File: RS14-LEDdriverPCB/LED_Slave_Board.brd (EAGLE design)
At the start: 63.2 x 38.1 mm, 26 parts, among them U1 PIC32MX250F128B-I/SP

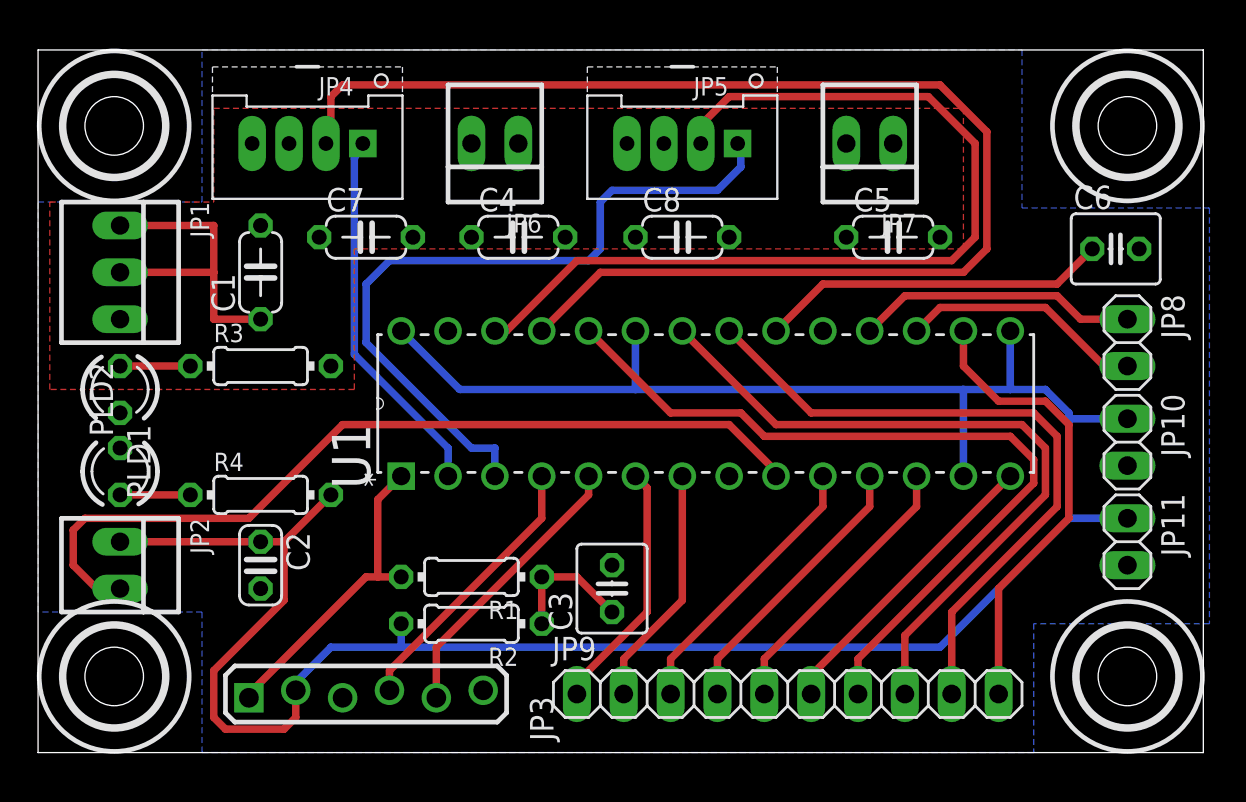
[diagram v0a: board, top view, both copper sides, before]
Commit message: Revised Board and Schematic
Changed capacitor footprints and screw hole placement
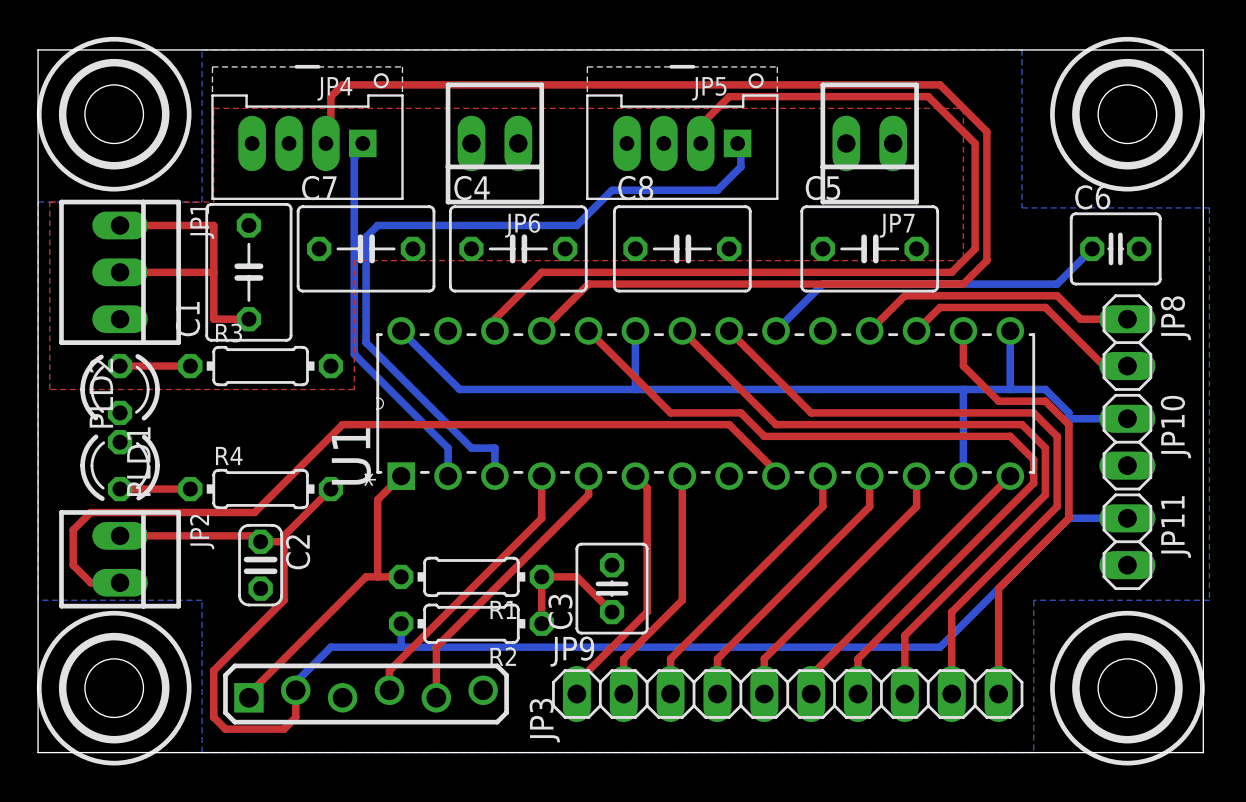
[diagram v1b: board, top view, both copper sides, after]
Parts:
- C1, C4, C5, C7, C8: device rcl:C050-024X044 -> rcl:C050-045X075
- moved C5 1.42 mm to (45.1, 27.3)
- moved C4 0.64 mm to (26.0, 27.3)
- moved C7 0.64 mm to (17.8, 27.3)
- moved C8 0.64 mm to (34.9, 27.3)
- moved C1 0.63 mm to (11.4, 26.0)
- moved JP2 0.32 mm to (4.45, 10.5)
- moved PLD2 0.32 mm to (4.45, 15.6)
- moved R4 0.32 mm to (12.1, 14.3)
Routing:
- net SCK2: track 50.8 -> 51.5 mm
- net 5V: track 17.8 -> 17.1 mm
